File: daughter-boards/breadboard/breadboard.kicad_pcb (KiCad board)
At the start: 2 copper layers, 30 x 92 mm, 54 parts, among them P1 SAMTEC-QSE-020-01-F-D-A, P2 SAMTEC-QSE-020-01-F-D-A

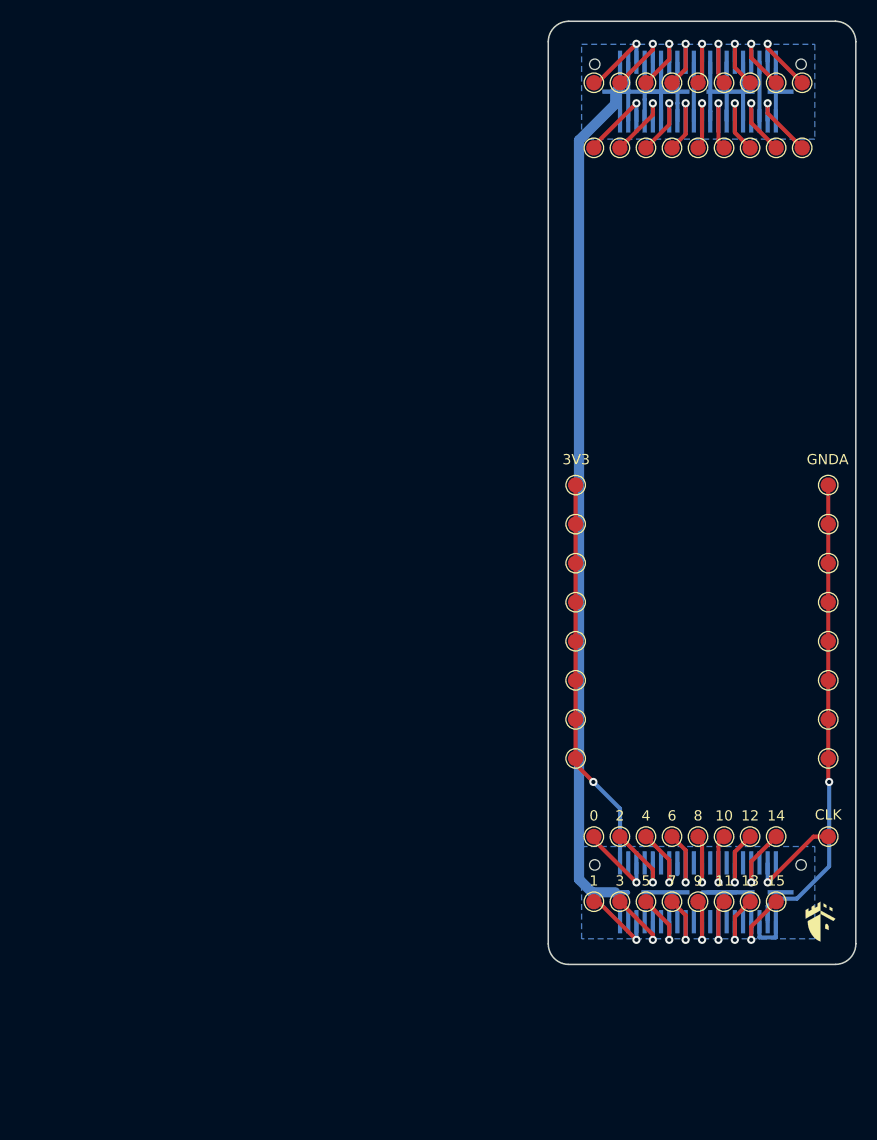
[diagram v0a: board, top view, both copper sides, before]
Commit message: Updated daughterboards for the new Scaffold socket
Update breadboard, smartcard and STM32F205 daughterboards to fit the
new socket format of Scaffold v1.1 hardware.
Previous socket format is now deprecated.
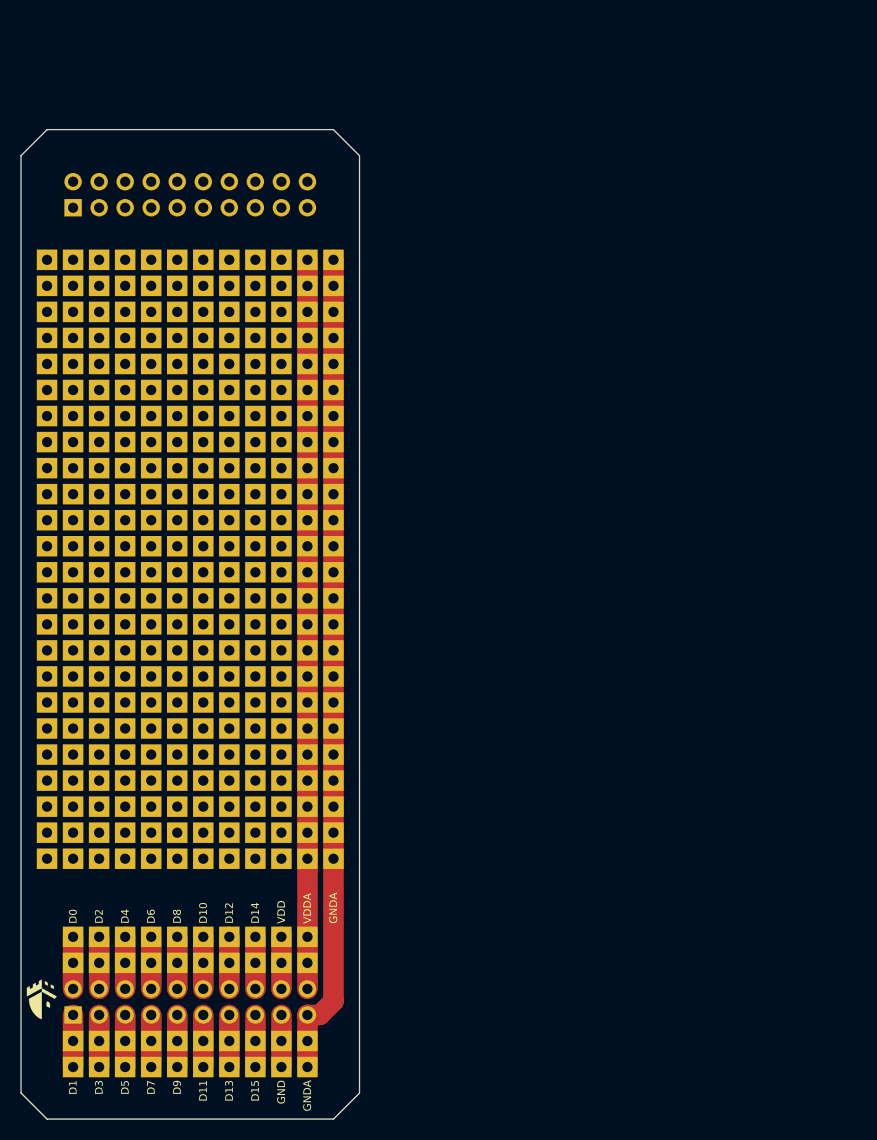
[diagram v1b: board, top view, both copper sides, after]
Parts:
- removed G***: LOGO, mykicadlibs:donjon-3000
- removed P1, P2: SAMTEC-QSE-020-01-F-D-A, mykicadlibs:SAMTEC-QSE-020-01-F-D-A
- added J1: Conn_02x10_Odd_Even, Connector_PinSocket_2.54mm:PinSocket_2x10_P2.54mm_Vertical, B.Cu at (50.8, 154.9)
- added J2: Conn_02x10_Odd_Even, Connector_PinSocket_2.54mm:PinSocket_2x10_P2.54mm_Vertical, B.Cu at (50.8, 76.2)
- added LOGO1: DUNGEON_LOGO, mykicadlibs:donjon-3000, F.Cu at (47.8, 153.4)
- added TP100: TestPoint, mykicadlibs:TEST_BREADBOARD_RECTANGULAR, F.Cu at (48.3, 81.3)
- added TP101: TestPoint, mykicadlibs:TEST_BREADBOARD_RECTANGULAR, F.Cu at (50.8, 96.5)
- added TP102: TestPoint, mykicadlibs:TEST_BREADBOARD_RECTANGULAR, F.Cu at (50.8, 86.4)
- added TP103: TestPoint, mykicadlibs:TEST_BREADBOARD_RECTANGULAR, F.Cu at (50.8, 116.8)
- added TP104: TestPoint, mykicadlibs:TEST_BREADBOARD_RECTANGULAR, F.Cu at (50.8, 101.6)
- added TP105: TestPoint, mykicadlibs:TEST_BREADBOARD_RECTANGULAR, F.Cu at (50.8, 88.9)
- added TP106: TestPoint, mykicadlibs:TEST_BREADBOARD_RECTANGULAR, F.Cu at (50.8, 91.4)
- added TP107: TestPoint, mykicadlibs:TEST_BREADBOARD_RECTANGULAR, F.Cu at (50.8, 111.8)
- added TP108: TestPoint, mykicadlibs:TEST_BREADBOARD_RECTANGULAR, F.Cu at (50.8, 121.9)
- added TP109: TestPoint, mykicadlibs:TEST_BREADBOARD_RECTANGULAR, F.Cu at (50.8, 129.5)
- added TP110: TestPoint, mykicadlibs:TEST_BREADBOARD_RECTANGULAR, F.Cu at (50.8, 81.3)
- added TP111: TestPoint, mykicadlibs:TEST_BREADBOARD_RECTANGULAR, F.Cu at (50.8, 99.1)
- added TP112: TestPoint, mykicadlibs:TEST_BREADBOARD_RECTANGULAR, F.Cu at (50.8, 119.4)
- added TP113: TestPoint, mykicadlibs:TEST_BREADBOARD_RECTANGULAR, F.Cu at (50.8, 124.5)
- added TP114: TestPoint, mykicadlibs:TEST_BREADBOARD_RECTANGULAR, F.Cu at (50.8, 94.0)
- added TP115: TestPoint, mykicadlibs:TEST_BREADBOARD_RECTANGULAR, F.Cu at (50.8, 104.1)
- added TP116: TestPoint, mykicadlibs:TEST_BREADBOARD_RECTANGULAR, F.Cu at (50.8, 114.3)
- added TP117: TestPoint, mykicadlibs:TEST_BREADBOARD_RECTANGULAR, F.Cu at (50.8, 127.0)
- added TP118: TestPoint, mykicadlibs:TEST_BREADBOARD_RECTANGULAR, F.Cu at (50.8, 83.8)
- added TP119: TestPoint, mykicadlibs:TEST_BREADBOARD_RECTANGULAR, F.Cu at (50.8, 106.7)
- added TP120: TestPoint, mykicadlibs:TEST_BREADBOARD_RECTANGULAR, F.Cu at (50.8, 109.2)
- added TP121: TestPoint, mykicadlibs:TEST_BREADBOARD_RECTANGULAR, F.Cu at (53.3, 91.4)
- added TP122: TestPoint, mykicadlibs:TEST_BREADBOARD_RECTANGULAR, F.Cu at (53.3, 114.3)
- added TP123: TestPoint, mykicadlibs:TEST_BREADBOARD_RECTANGULAR, F.Cu at (53.3, 88.9)
- added TP124: TestPoint, mykicadlibs:TEST_BREADBOARD_RECTANGULAR, F.Cu at (53.3, 94.0)
- added TP125: TestPoint, mykicadlibs:TEST_BREADBOARD_RECTANGULAR, F.Cu at (53.3, 121.9)
- added TP126: TestPoint, mykicadlibs:TEST_BREADBOARD_RECTANGULAR, F.Cu at (53.3, 116.8)
- added TP127: TestPoint, mykicadlibs:TEST_BREADBOARD_RECTANGULAR, F.Cu at (53.3, 104.1)
- added TP128: TestPoint, mykicadlibs:TEST_BREADBOARD_RECTANGULAR, F.Cu at (53.3, 86.4)
- added TP129: TestPoint, mykicadlibs:TEST_BREADBOARD_RECTANGULAR, F.Cu at (53.3, 127.0)
- added TP130: TestPoint, mykicadlibs:TEST_BREADBOARD_RECTANGULAR, F.Cu at (53.3, 111.8)
- added TP131: TestPoint, mykicadlibs:TEST_BREADBOARD_RECTANGULAR, F.Cu at (53.3, 96.5)
- added TP132: TestPoint, mykicadlibs:TEST_BREADBOARD_RECTANGULAR, F.Cu at (53.3, 83.8)
- added TP133: TestPoint, mykicadlibs:TEST_BREADBOARD_RECTANGULAR, F.Cu at (53.3, 124.5)
- added TP134: TestPoint, mykicadlibs:TEST_BREADBOARD_RECTANGULAR, F.Cu at (53.3, 119.4)
- added TP135: TestPoint, mykicadlibs:TEST_BREADBOARD_RECTANGULAR, F.Cu at (53.3, 101.6)
- added TP136: TestPoint, mykicadlibs:TEST_BREADBOARD_RECTANGULAR, F.Cu at (53.3, 81.3)
- added TP137: TestPoint, mykicadlibs:TEST_BREADBOARD_RECTANGULAR, F.Cu at (53.3, 129.5)
- added TP138: TestPoint, mykicadlibs:TEST_BREADBOARD_RECTANGULAR, F.Cu at (53.3, 106.7)
- added TP139: TestPoint, mykicadlibs:TEST_BREADBOARD_RECTANGULAR, F.Cu at (53.3, 109.2)
- added TP140: TestPoint, mykicadlibs:TEST_BREADBOARD_RECTANGULAR, F.Cu at (53.3, 99.1)
- added TP141: TestPoint, mykicadlibs:TEST_BREADBOARD_RECTANGULAR, F.Cu at (55.9, 116.8)
- added TP142: TestPoint, mykicadlibs:TEST_BREADBOARD_RECTANGULAR, F.Cu at (55.9, 94.0)
- added TP143: TestPoint, mykicadlibs:TEST_BREADBOARD_RECTANGULAR, F.Cu at (55.9, 109.2)
- added TP144: TestPoint, mykicadlibs:TEST_BREADBOARD_RECTANGULAR, F.Cu at (55.9, 104.1)
- added TP145: TestPoint, mykicadlibs:TEST_BREADBOARD_RECTANGULAR, F.Cu at (55.9, 83.8)
- added TP146: TestPoint, mykicadlibs:TEST_BREADBOARD_RECTANGULAR, F.Cu at (55.9, 127.0)
- added TP147: TestPoint, mykicadlibs:TEST_BREADBOARD_RECTANGULAR, F.Cu at (55.9, 114.3)
- added TP148: TestPoint, mykicadlibs:TEST_BREADBOARD_RECTANGULAR, F.Cu at (55.9, 106.7)
- added TP149: TestPoint, mykicadlibs:TEST_BREADBOARD_RECTANGULAR, F.Cu at (55.9, 86.4)
- added TP150: TestPoint, mykicadlibs:TEST_BREADBOARD_RECTANGULAR, F.Cu at (55.9, 124.5)
- added TP151: TestPoint, mykicadlibs:TEST_BREADBOARD_RECTANGULAR, F.Cu at (55.9, 91.4)
- added TP152: TestPoint, mykicadlibs:TEST_BREADBOARD_RECTANGULAR, F.Cu at (55.9, 101.6)
- added TP153: TestPoint, mykicadlibs:TEST_BREADBOARD_RECTANGULAR, F.Cu at (55.9, 88.9)
- added TP154: TestPoint, mykicadlibs:TEST_BREADBOARD_RECTANGULAR, F.Cu at (55.9, 129.5)
- added TP155: TestPoint, mykicadlibs:TEST_BREADBOARD_RECTANGULAR, F.Cu at (55.9, 111.8)
- added TP156: TestPoint, mykicadlibs:TEST_BREADBOARD_RECTANGULAR, F.Cu at (55.9, 99.1)
- added TP157: TestPoint, mykicadlibs:TEST_BREADBOARD_RECTANGULAR, F.Cu at (55.9, 96.5)
- added TP158: TestPoint, mykicadlibs:TEST_BREADBOARD_RECTANGULAR, F.Cu at (55.9, 121.9)
- added TP159: TestPoint, mykicadlibs:TEST_BREADBOARD_RECTANGULAR, F.Cu at (55.9, 81.3)
- added TP160: TestPoint, mykicadlibs:TEST_BREADBOARD_RECTANGULAR, F.Cu at (55.9, 119.4)
- added TP161: TestPoint, mykicadlibs:TEST_BREADBOARD_RECTANGULAR, F.Cu at (58.4, 114.3)
- added TP162: TestPoint, mykicadlibs:TEST_BREADBOARD_RECTANGULAR, F.Cu at (58.4, 101.6)
- added TP163: TestPoint, mykicadlibs:TEST_BREADBOARD_RECTANGULAR, F.Cu at (58.4, 91.4)
- added TP164: TestPoint, mykicadlibs:TEST_BREADBOARD_RECTANGULAR, F.Cu at (58.4, 127.0)
- added TP165: TestPoint, mykicadlibs:TEST_BREADBOARD_RECTANGULAR, F.Cu at (58.4, 116.8)
- added TP166: TestPoint, mykicadlibs:TEST_BREADBOARD_RECTANGULAR, F.Cu at (58.4, 96.5)
- added TP167: TestPoint, mykicadlibs:TEST_BREADBOARD_RECTANGULAR, F.Cu at (58.4, 83.8)
- added TP168: TestPoint, mykicadlibs:TEST_BREADBOARD_RECTANGULAR, F.Cu at (58.4, 124.5)
- added TP169: TestPoint, mykicadlibs:TEST_BREADBOARD_RECTANGULAR, F.Cu at (58.4, 111.8)
- added TP170: TestPoint, mykicadlibs:TEST_BREADBOARD_RECTANGULAR, F.Cu at (58.4, 104.1)
- added TP171: TestPoint, mykicadlibs:TEST_BREADBOARD_RECTANGULAR, F.Cu at (58.4, 99.1)
- added TP172: TestPoint, mykicadlibs:TEST_BREADBOARD_RECTANGULAR, F.Cu at (58.4, 81.3)
- added TP173: TestPoint, mykicadlibs:TEST_BREADBOARD_RECTANGULAR, F.Cu at (58.4, 121.9)
- added TP174: TestPoint, mykicadlibs:TEST_BREADBOARD_RECTANGULAR, F.Cu at (58.4, 109.2)
- added TP175: TestPoint, mykicadlibs:TEST_BREADBOARD_RECTANGULAR, F.Cu at (58.4, 106.7)
- added TP176: TestPoint, mykicadlibs:TEST_BREADBOARD_RECTANGULAR, F.Cu at (58.4, 88.9)
- added TP177: TestPoint, mykicadlibs:TEST_BREADBOARD_RECTANGULAR, F.Cu at (58.4, 129.5)
- added TP178: TestPoint, mykicadlibs:TEST_BREADBOARD_RECTANGULAR, F.Cu at (58.4, 94.0)
- added TP179: TestPoint, mykicadlibs:TEST_BREADBOARD_RECTANGULAR, F.Cu at (58.4, 119.4)
- added TP180: TestPoint, mykicadlibs:TEST_BREADBOARD_RECTANGULAR, F.Cu at (58.4, 86.4)
- added TP181: TestPoint, mykicadlibs:TEST_BREADBOARD_RECTANGULAR, F.Cu at (61.0, 96.5)
- added TP182: TestPoint, mykicadlibs:TEST_BREADBOARD_RECTANGULAR, F.Cu at (61.0, 111.8)
- added TP183: TestPoint, mykicadlibs:TEST_BREADBOARD_RECTANGULAR, F.Cu at (61.0, 101.6)
- added TP184: TestPoint, mykicadlibs:TEST_BREADBOARD_RECTANGULAR, F.Cu at (61.0, 91.4)
- added TP185: TestPoint, mykicadlibs:TEST_BREADBOARD_RECTANGULAR, F.Cu at (61.0, 121.9)
- added TP186: TestPoint, mykicadlibs:TEST_BREADBOARD_RECTANGULAR, F.Cu at (61.0, 114.3)
- added TP187: TestPoint, mykicadlibs:TEST_BREADBOARD_RECTANGULAR, F.Cu at (61.0, 81.3)
- added TP188: TestPoint, mykicadlibs:TEST_BREADBOARD_RECTANGULAR, F.Cu at (61.0, 94.0)
- added TP189: TestPoint, mykicadlibs:TEST_BREADBOARD_RECTANGULAR, F.Cu at (61.0, 86.4)
- added TP190: TestPoint, mykicadlibs:TEST_BREADBOARD_RECTANGULAR, F.Cu at (61.0, 127.0)
- added TP191: TestPoint, mykicadlibs:TEST_BREADBOARD_RECTANGULAR, F.Cu at (61.0, 119.4)
- added TP192: TestPoint, mykicadlibs:TEST_BREADBOARD_RECTANGULAR, F.Cu at (61.0, 99.1)
- added TP193: TestPoint, mykicadlibs:TEST_BREADBOARD_RECTANGULAR, F.Cu at (61.0, 83.8)
- added TP194: TestPoint, mykicadlibs:TEST_BREADBOARD_RECTANGULAR, F.Cu at (61.0, 124.5)
- added TP195: TestPoint, mykicadlibs:TEST_BREADBOARD_RECTANGULAR, F.Cu at (61.0, 109.2)
- added TP196: TestPoint, mykicadlibs:TEST_BREADBOARD_RECTANGULAR, F.Cu at (61.0, 106.7)
- added TP197: TestPoint, mykicadlibs:TEST_BREADBOARD_RECTANGULAR, F.Cu at (61.0, 88.9)
- added TP198: TestPoint, mykicadlibs:TEST_BREADBOARD_RECTANGULAR, F.Cu at (61.0, 129.5)
- added TP199: TestPoint, mykicadlibs:TEST_BREADBOARD_RECTANGULAR, F.Cu at (61.0, 104.1)
- added TP200: TestPoint, mykicadlibs:TEST_BREADBOARD_RECTANGULAR, F.Cu at (61.0, 116.8)
- added TP201: TestPoint, mykicadlibs:TEST_BREADBOARD_RECTANGULAR, F.Cu at (63.5, 114.3)
- added TP202: TestPoint, mykicadlibs:TEST_BREADBOARD_RECTANGULAR, F.Cu at (63.5, 99.1)
- added TP203: TestPoint, mykicadlibs:TEST_BREADBOARD_RECTANGULAR, F.Cu at (63.5, 88.9)
- added TP204: TestPoint, mykicadlibs:TEST_BREADBOARD_RECTANGULAR, F.Cu at (63.5, 96.5)
- added TP205: TestPoint, mykicadlibs:TEST_BREADBOARD_RECTANGULAR, F.Cu at (63.5, 119.4)
- added TP206: TestPoint, mykicadlibs:TEST_BREADBOARD_RECTANGULAR, F.Cu at (63.5, 109.2)
- added TP207: TestPoint, mykicadlibs:TEST_BREADBOARD_RECTANGULAR, F.Cu at (63.5, 106.7)
- added TP208: TestPoint, mykicadlibs:TEST_BREADBOARD_RECTANGULAR, F.Cu at (63.5, 81.3)
- added TP209: TestPoint, mykicadlibs:TEST_BREADBOARD_RECTANGULAR, F.Cu at (63.5, 124.5)
- added TP210: TestPoint, mykicadlibs:TEST_BREADBOARD_RECTANGULAR, F.Cu at (63.5, 111.8)
- added TP211: TestPoint, mykicadlibs:TEST_BREADBOARD_RECTANGULAR, F.Cu at (63.5, 104.1)
- added TP212: TestPoint, mykicadlibs:TEST_BREADBOARD_RECTANGULAR, F.Cu at (63.5, 86.4)
- added TP213: TestPoint, mykicadlibs:TEST_BREADBOARD_RECTANGULAR, F.Cu at (63.5, 121.9)
- added TP214: TestPoint, mykicadlibs:TEST_BREADBOARD_RECTANGULAR, F.Cu at (63.5, 129.5)
- added TP215: TestPoint, mykicadlibs:TEST_BREADBOARD_RECTANGULAR, F.Cu at (63.5, 101.6)
- added TP216: TestPoint, mykicadlibs:TEST_BREADBOARD_RECTANGULAR, F.Cu at (63.5, 91.4)
- added TP217: TestPoint, mykicadlibs:TEST_BREADBOARD_RECTANGULAR, F.Cu at (63.5, 127.0)
- added TP218: TestPoint, mykicadlibs:TEST_BREADBOARD_RECTANGULAR, F.Cu at (63.5, 94.0)
- added TP219: TestPoint, mykicadlibs:TEST_BREADBOARD_RECTANGULAR, F.Cu at (63.5, 116.8)
- added TP220: TestPoint, mykicadlibs:TEST_BREADBOARD_RECTANGULAR, F.Cu at (63.5, 83.8)
- added TP221: TestPoint, mykicadlibs:TEST_BREADBOARD_RECTANGULAR, F.Cu at (66.0, 81.3)
- added TP222: TestPoint, mykicadlibs:TEST_BREADBOARD_RECTANGULAR, F.Cu at (66.0, 119.4)
- added TP223: TestPoint, mykicadlibs:TEST_BREADBOARD_RECTANGULAR, F.Cu at (66.0, 96.5)
- added TP224: TestPoint, mykicadlibs:TEST_BREADBOARD_RECTANGULAR, F.Cu at (66.0, 83.8)
- added TP225: TestPoint, mykicadlibs:TEST_BREADBOARD_RECTANGULAR, F.Cu at (66.0, 111.8)
- added TP226: TestPoint, mykicadlibs:TEST_BREADBOARD_RECTANGULAR, F.Cu at (66.0, 91.4)
- added TP227: TestPoint, mykicadlibs:TEST_BREADBOARD_RECTANGULAR, F.Cu at (66.0, 129.5)
- added TP228: TestPoint, mykicadlibs:TEST_BREADBOARD_RECTANGULAR, F.Cu at (66.0, 94.0)
- added TP229: TestPoint, mykicadlibs:TEST_BREADBOARD_RECTANGULAR, F.Cu at (66.0, 104.1)
- added TP230: TestPoint, mykicadlibs:TEST_BREADBOARD_RECTANGULAR, F.Cu at (66.0, 114.3)
- added TP231: TestPoint, mykicadlibs:TEST_BREADBOARD_RECTANGULAR, F.Cu at (66.0, 121.9)
- added TP232: TestPoint, mykicadlibs:TEST_BREADBOARD_RECTANGULAR, F.Cu at (66.0, 88.9)
- added TP233: TestPoint, mykicadlibs:TEST_BREADBOARD_RECTANGULAR, F.Cu at (66.0, 99.1)
- added TP234: TestPoint, mykicadlibs:TEST_BREADBOARD_RECTANGULAR, F.Cu at (66.0, 109.2)
- added TP235: TestPoint, mykicadlibs:TEST_BREADBOARD_RECTANGULAR, F.Cu at (66.0, 124.5)
- added TP236: TestPoint, mykicadlibs:TEST_BREADBOARD_RECTANGULAR, F.Cu at (66.0, 86.4)
- added TP237: TestPoint, mykicadlibs:TEST_BREADBOARD_RECTANGULAR, F.Cu at (66.0, 101.6)
- added TP238: TestPoint, mykicadlibs:TEST_BREADBOARD_RECTANGULAR, F.Cu at (66.0, 116.8)
- added TP239: TestPoint, mykicadlibs:TEST_BREADBOARD_RECTANGULAR, F.Cu at (66.0, 106.7)
- added TP240: TestPoint, mykicadlibs:TEST_BREADBOARD_RECTANGULAR, F.Cu at (66.0, 127.0)
- added TP241: TestPoint, mykicadlibs:TEST_BREADBOARD_RECTANGULAR, F.Cu at (68.6, 83.8)
- added TP242: TestPoint, mykicadlibs:TEST_BREADBOARD_RECTANGULAR, F.Cu at (68.6, 99.1)
- added TP243: TestPoint, mykicadlibs:TEST_BREADBOARD_RECTANGULAR, F.Cu at (68.6, 116.8)
- added TP244: TestPoint, mykicadlibs:TEST_BREADBOARD_RECTANGULAR, F.Cu at (68.6, 94.0)
- added TP245: TestPoint, mykicadlibs:TEST_BREADBOARD_RECTANGULAR, F.Cu at (68.6, 127.0)
- added TP246: TestPoint, mykicadlibs:TEST_BREADBOARD_RECTANGULAR, F.Cu at (68.6, 114.3)
- added TP247: TestPoint, mykicadlibs:TEST_BREADBOARD_RECTANGULAR, F.Cu at (68.6, 129.5)
- added TP248: TestPoint, mykicadlibs:TEST_BREADBOARD_RECTANGULAR, F.Cu at (68.6, 88.9)
- added TP249: TestPoint, mykicadlibs:TEST_BREADBOARD_RECTANGULAR, F.Cu at (68.6, 104.1)
- added TP250: TestPoint, mykicadlibs:TEST_BREADBOARD_RECTANGULAR, F.Cu at (68.6, 111.8)
- added TP251: TestPoint, mykicadlibs:TEST_BREADBOARD_RECTANGULAR, F.Cu at (68.6, 124.5)
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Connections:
- TP1 pad 1: Net-(P1-Pad4) -> VDDA
- TP10 pad 1: Net-(P1-Pad8) -> VDDA
- TP11 pad 1: Net-(P1-Pad12) -> VDDA
- TP12 pad 1: Net-(P1-Pad16) -> VDDA
- TP13 pad 1: Net-(P1-Pad20) -> VDDA
- TP14 pad 1: Net-(P1-Pad24) -> VDDA
- TP15 pad 1: Net-(P1-Pad28) -> VDDA
- TP16 pad 1: Net-(P1-Pad32) -> VDDA
- TP17 pad 1: Net-(P1-Pad36) -> VDDA
- TP18 pad 1: GNDA -> VDDA
- TP19 pad 1: GNDA -> VDDA
- TP2 pad 1: Net-(P1-Pad7) -> VDDA
- TP20 pad 1: GNDA -> VDDA
- TP21 pad 1: GNDA -> /D2
- TP22 pad 1: GNDA -> /D2
- TP23 pad 1: GNDA -> /D3
- TP24 pad 1: GNDA -> /D3
- TP25 pad 1: GNDA -> /D4
- TP26 pad 1: +3V3 -> /D4
- TP27 pad 1: +3V3 -> GNDA
- TP28 pad 1: +3V3 -> GNDA
- TP29 pad 1: +3V3 -> GNDA
- TP3 pad 1: Net-(P1-Pad11) -> VDDA
- TP30 pad 1: +3V3 -> GNDA
- TP31 pad 1: +3V3 -> GNDA
- TP32 pad 1: +3V3 -> GNDA
- TP33 pad 1: +3V3 -> GNDA
- TP34 pad 1: Net-(P2-Pad3) -> GNDA
- TP35 pad 1: Net-(P2-Pad7) -> GNDA
- TP36 pad 1: Net-(P2-Pad11) -> GNDA
- TP37 pad 1: Net-(P2-Pad15) -> GNDA
- TP38 pad 1: Net-(P2-Pad19) -> GNDA
- TP39 pad 1: Net-(P2-Pad23) -> GNDA
- TP4 pad 1: Net-(P1-Pad15) -> VDDA
- TP40 pad 1: Net-(P2-Pad27) -> GNDA
- TP41 pad 1: Net-(P2-Pad31) -> GNDA
- TP42 pad 1: Net-(P2-Pad35) -> GNDA
- TP43 pad 1: Net-(P2-Pad4) -> GNDA
- TP44 pad 1: Net-(P2-Pad8) -> GNDA
- TP45 pad 1: Net-(P2-Pad12) -> GNDA
- TP46 pad 1: Net-(P2-Pad16) -> GNDA
- TP47 pad 1: Net-(P2-Pad20) -> /D5
- TP48 pad 1: Net-(P2-Pad24) -> /D5
- TP49 pad 1: Net-(P2-Pad28) -> /D6
- TP5 pad 1: Net-(P1-Pad19) -> VDDA
- TP50 pad 1: Net-(P2-Pad32) -> /D6
- TP51 pad 1: Net-(P2-Pad36) -> /D7
- TP6 pad 1: Net-(P1-Pad23) -> VDDA
- TP7 pad 1: Net-(P1-Pad27) -> VDDA
- TP8 pad 1: Net-(P1-Pad31) -> VDDA
- TP9 pad 1: Net-(P1-Pad35) -> VDDA
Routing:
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- removed copper zone on B.Cu, net GND
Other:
- board size 30 x 92 mm -> 33 x 96.5 mm
- rule pad_to_mask_clearance: 0.2 -> 0
- board text added: "D0"
- board text added: "D1"
- board text added: "D10"
- board text added: "D11"
- board text added: "D12"
- board text added: "D13"
- board text added: "D14"
- board text added: "D15"
- board text added: "D2"
- board text added: "D3"
- board text added: "D4"
- board text added: "D5"
- board text added: "D6"
- board text added: "D7"
- board text added: "D8"
- board text added: "D9"
- board text added: "GND"
- board text added: "VDD"
- board text added: "VDDA"
- board text removed: "0"
- board text removed: "1"
- board text removed: "10"
- board text removed: "11"
- board text removed: "12"
- board text removed: "13"
- board text removed: "14"
- board text removed: "15"
- board text removed: "2"
- board text removed: "3"
- board text removed: "3V3"
- board text removed: "4"
- board text removed: "5"
- board text removed: "6"
- board text removed: "7"
- board text removed: "8"
- board text removed: "9"
- board text removed: "CLK"

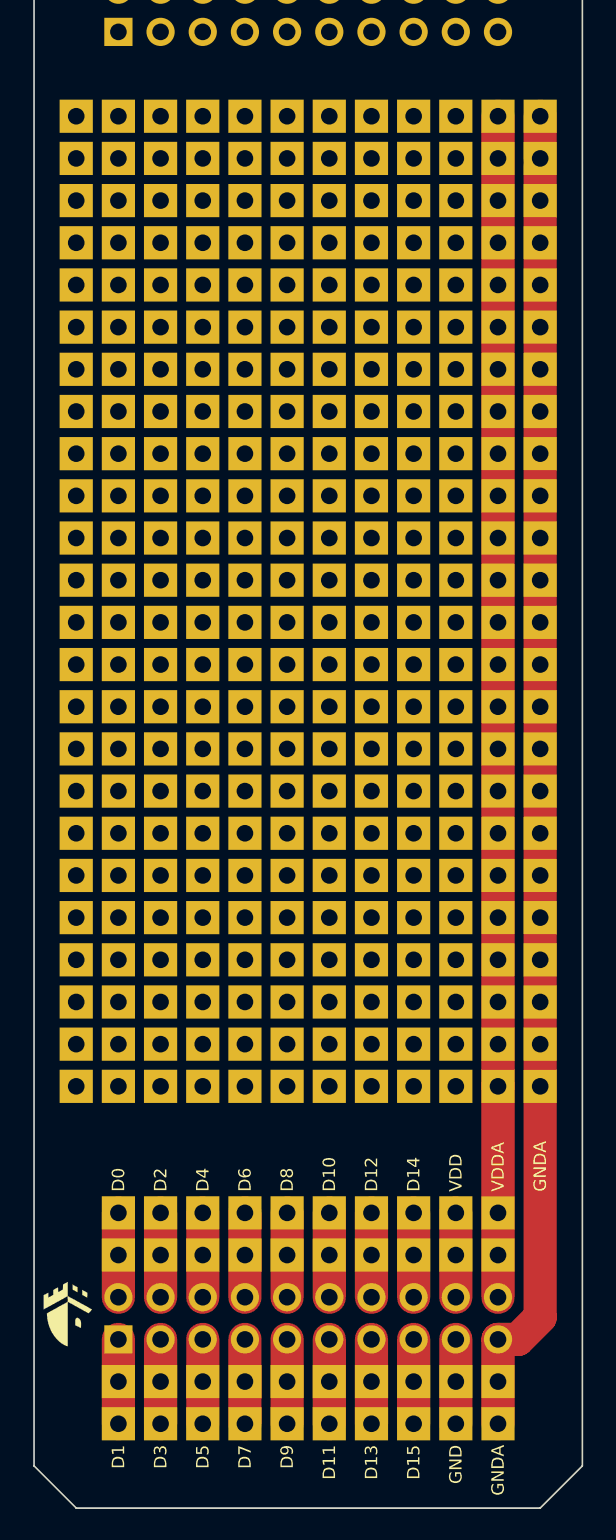
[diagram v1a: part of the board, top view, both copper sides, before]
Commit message: Fixed holes in breadboard daughterboard.
Replaced plated holes with non-plated holes for easier solderability.
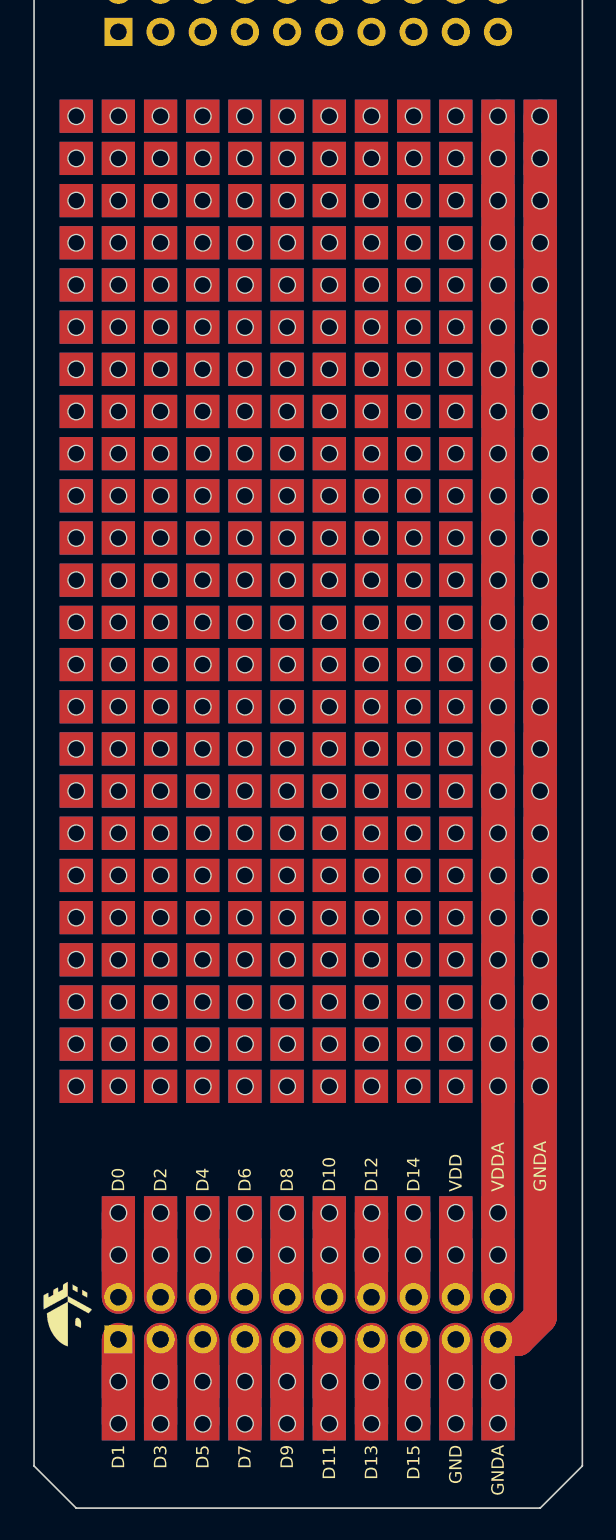
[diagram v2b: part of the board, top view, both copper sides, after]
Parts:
- removed TP1, TP10, TP100, TP101, TP102, TP103, TP104, TP105, TP106, TP107, TP108, TP109, TP11, TP110, TP111, TP112, TP113, TP114, TP115, TP116, TP117, TP118, TP119, TP12, TP120, TP121, TP122, TP123, TP124, TP125, TP126, TP127, TP128, TP129, TP13, TP130, TP131, TP132, TP133, TP134, TP135, TP136, TP137, TP138, TP139, TP14, TP140, TP141, TP142, TP143, TP144, TP145, TP146, TP147, TP148, TP149, TP15, TP150, TP151, TP152, TP153, TP154, TP155, TP156, TP157, TP158, TP159, TP16, TP160, TP161, TP162, TP163, TP164, TP165, TP166, TP167, TP168, TP169, TP17, TP170, TP171, TP172, TP173, TP174, TP175, TP176, TP177, TP178, TP179, TP18, TP180, TP181, TP182, TP183, TP184, TP185, TP186, TP187, TP188, TP189, TP19, TP190, TP191, TP192, TP193, TP194, TP195, TP196, TP197, TP198, TP199, TP2, TP20, TP200, TP201, TP202, TP203, TP204, TP205, TP206, TP207, TP208, TP209, TP21, TP210, TP211, TP212, TP213, TP214, TP215, TP216, TP217, TP218, TP219, TP22, TP220, TP221, TP222, TP223, TP224, TP225, TP226, TP227, TP228, TP229, TP23, TP230, TP231, TP232, TP233, TP234, TP235, TP236, TP237, TP238, TP239, TP24, TP240, TP241, TP242, TP243, TP244, TP245, TP246, TP247, TP248, TP249, TP25, TP250, TP251, TP252, TP253, TP254, TP255, TP256, TP257, TP258, TP259, TP26, TP260, TP261, TP262, TP263, TP264, TP265, TP266, TP267, TP268, TP269, TP27, TP270, TP271, TP272, TP273, TP274, TP275, TP276, TP277, TP278, TP279, TP28, TP280, TP281, TP282, TP283, TP284, TP285, TP286, TP287, TP288, TP289, TP29, TP290, TP291, TP292, TP293, TP294, TP295, TP296, TP297, TP298, TP299, TP3, TP30, TP300, TP301, TP302, TP303, TP304, TP305, TP306, TP307, TP308, TP309, TP31, TP310, TP311, TP312, TP313, TP314, TP315, TP316, TP317, TP318, TP319, TP32, TP320, TP321, TP322, TP323, TP324, TP325, TP326, TP327, TP328, TP33, TP34, TP35, TP36, TP37, TP38, TP39, TP4, TP40, TP41, TP42, TP43, TP44, TP45, TP46, TP47, TP48, TP49, TP5, TP50, TP51, TP52, TP53, TP54, TP55, TP56, TP57, TP58, TP59, TP6, TP60, TP61, TP62, TP63, TP64, TP65, TP66, TP67, TP68, TP69, TP7, TP70, TP71, TP72, TP73, TP74, TP75, TP76, TP77, TP78, TP79, TP8, TP80, TP81, TP82, TP83, TP84, TP85, TP86, TP87, TP88, TP89, TP9, TP90, TP91, TP92, TP93, TP94, TP95, TP96, TP97, TP98, TP99: TestPoint, mykicadlibs:TEST_BREADBOARD_RECTANGULAR
- added U1: BREADBOARD_NPTH, mykicadlibs:TEST_BREADBOARD_RECTANGULAR_NPTH2, F.Cu at (48.3, 83.8)
- added U10: BREADBOARD_NPTH, mykicadlibs:TEST_BREADBOARD_RECTANGULAR_NPTH2, F.Cu at (48.3, 96.5)
- added U100: BREADBOARD_NPTH, mykicadlibs:TEST_BREADBOARD_RECTANGULAR_NPTH2, F.Cu at (66.0, 81.3)
- added U101: BREADBOARD_NPTH, mykicadlibs:TEST_BREADBOARD_RECTANGULAR_NPTH2, F.Cu at (71.1, 139.7)
- added U102: BREADBOARD_NPTH, mykicadlibs:TEST_BREADBOARD_RECTANGULAR_NPTH2, F.Cu at (48.3, 116.8)
- added U103: BREADBOARD_NPTH, mykicadlibs:TEST_BREADBOARD_RECTANGULAR_NPTH2, F.Cu at (50.8, 134.6)
- added U104: BREADBOARD_NPTH, mykicadlibs:TEST_BREADBOARD_RECTANGULAR_NPTH2, F.Cu at (50.8, 86.4)
- added U105: BREADBOARD_NPTH, mykicadlibs:TEST_BREADBOARD_RECTANGULAR_NPTH2, F.Cu at (53.3, 83.8)
- added U106: BREADBOARD_NPTH, mykicadlibs:TEST_BREADBOARD_RECTANGULAR_NPTH2, F.Cu at (48.3, 109.2)
- added U107: BREADBOARD_NPTH, mykicadlibs:TEST_BREADBOARD_RECTANGULAR_NPTH2, F.Cu at (53.3, 101.6)
- added U108: BREADBOARD_NPTH, mykicadlibs:TEST_BREADBOARD_RECTANGULAR_NPTH2, F.Cu at (63.5, 86.4)
- added U109: BREADBOARD_NPTH, mykicadlibs:TEST_BREADBOARD_RECTANGULAR_NPTH2, F.Cu at (61.0, 111.8)
- added U11: BREADBOARD_NPTH, mykicadlibs:TEST_BREADBOARD_RECTANGULAR_NPTH2, F.Cu at (71.1, 104.1)
- added U110: BREADBOARD_NPTH, mykicadlibs:TEST_BREADBOARD_RECTANGULAR_NPTH2, F.Cu at (63.5, 94.0)
- added U111: BREADBOARD_NPTH, mykicadlibs:TEST_BREADBOARD_RECTANGULAR_NPTH2, F.Cu at (66.0, 104.1)
- added U112: BREADBOARD_NPTH, mykicadlibs:TEST_BREADBOARD_RECTANGULAR_NPTH2, F.Cu at (68.6, 124.5)
- added U113: BREADBOARD_NPTH, mykicadlibs:TEST_BREADBOARD_RECTANGULAR_NPTH2, F.Cu at (68.6, 88.9)
- added U114: BREADBOARD_NPTH, mykicadlibs:TEST_BREADBOARD_RECTANGULAR_NPTH2, F.Cu at (71.1, 83.8)
- added U115: BREADBOARD_NPTH, mykicadlibs:TEST_BREADBOARD_RECTANGULAR_NPTH2, F.Cu at (50.8, 132.1)
- added U116: BREADBOARD_NPTH, mykicadlibs:TEST_BREADBOARD_RECTANGULAR_NPTH2, F.Cu at (50.8, 94.0)
- added U117: BREADBOARD_NPTH, mykicadlibs:TEST_BREADBOARD_RECTANGULAR_NPTH2, F.Cu at (58.4, 94.0)
- added U118: BREADBOARD_NPTH, mykicadlibs:TEST_BREADBOARD_RECTANGULAR_NPTH2, F.Cu at (58.4, 114.3)
- added U119: BREADBOARD_NPTH, mykicadlibs:TEST_BREADBOARD_RECTANGULAR_NPTH2, F.Cu at (61.0, 129.5)
- added U12: BREADBOARD_NPTH, mykicadlibs:TEST_BREADBOARD_RECTANGULAR_NPTH2, F.Cu at (68.6, 111.8)
- added U120: BREADBOARD_NPTH, mykicadlibs:TEST_BREADBOARD_RECTANGULAR_NPTH2, F.Cu at (61.0, 88.9)
- added U121: BREADBOARD_NPTH, mykicadlibs:TEST_BREADBOARD_RECTANGULAR_NPTH2, F.Cu at (63.5, 104.1)
- added U122: BREADBOARD_NPTH, mykicadlibs:TEST_BREADBOARD_RECTANGULAR_NPTH2, F.Cu at (66.0, 129.5)
- added U123: BREADBOARD_NPTH, mykicadlibs:TEST_BREADBOARD_RECTANGULAR_NPTH2, F.Cu at (68.6, 114.3)
- added U124: BREADBOARD_NPTH, mykicadlibs:TEST_BREADBOARD_RECTANGULAR_NPTH2, F.Cu at (71.1, 114.3)
- added U125: BREADBOARD_NPTH, mykicadlibs:TEST_BREADBOARD_RECTANGULAR_NPTH2, F.Cu at (71.1, 94.0)
- added U126: BREADBOARD_NPTH, mykicadlibs:TEST_BREADBOARD_RECTANGULAR_NPTH2, F.Cu at (50.8, 119.4)
- added U127: BREADBOARD_NPTH, mykicadlibs:TEST_BREADBOARD_RECTANGULAR_NPTH2, F.Cu at (61.0, 99.1)
- added U128: BREADBOARD_NPTH, mykicadlibs:TEST_BREADBOARD_RECTANGULAR_NPTH2, F.Cu at (55.9, 134.6)
- added U129: BREADBOARD_NPTH, mykicadlibs:TEST_BREADBOARD_RECTANGULAR_NPTH2, F.Cu at (55.9, 101.6)
- added U13: BREADBOARD_NPTH, mykicadlibs:TEST_BREADBOARD_RECTANGULAR_NPTH2, F.Cu at (71.1, 119.4)
- added U130: BREADBOARD_NPTH, mykicadlibs:TEST_BREADBOARD_RECTANGULAR_NPTH2, F.Cu at (55.9, 86.4)
- added U131: BREADBOARD_NPTH, mykicadlibs:TEST_BREADBOARD_RECTANGULAR_NPTH2, F.Cu at (58.4, 106.7)
- added U132: BREADBOARD_NPTH, mykicadlibs:TEST_BREADBOARD_RECTANGULAR_NPTH2, F.Cu at (61.0, 94.0)
- added U133: BREADBOARD_NPTH, mykicadlibs:TEST_BREADBOARD_RECTANGULAR_NPTH2, F.Cu at (63.5, 119.4)
- added U134: BREADBOARD_NPTH, mykicadlibs:TEST_BREADBOARD_RECTANGULAR_NPTH2, F.Cu at (66.0, 106.7)
- added U135: BREADBOARD_NPTH, mykicadlibs:TEST_BREADBOARD_RECTANGULAR_NPTH2, F.Cu at (68.6, 137.2)
- added U136: BREADBOARD_NPTH, mykicadlibs:TEST_BREADBOARD_RECTANGULAR_NPTH2, F.Cu at (71.1, 109.2)
- added U137: BREADBOARD_NPTH, mykicadlibs:TEST_BREADBOARD_RECTANGULAR_NPTH2, F.Cu at (71.1, 101.6)
- added U138: BREADBOARD_NPTH, mykicadlibs:TEST_BREADBOARD_RECTANGULAR_NPTH2, F.Cu at (68.6, 127.0)
- added U139: BREADBOARD_NPTH, mykicadlibs:TEST_BREADBOARD_RECTANGULAR_NPTH2, F.Cu at (50.8, 88.9)
- added U14: BREADBOARD_NPTH, mykicadlibs:TEST_BREADBOARD_RECTANGULAR_NPTH2, F.Cu at (48.3, 137.2)
- added U140: BREADBOARD_NPTH, mykicadlibs:TEST_BREADBOARD_RECTANGULAR_NPTH2, F.Cu at (53.3, 134.6)
- added U141: BREADBOARD_NPTH, mykicadlibs:TEST_BREADBOARD_RECTANGULAR_NPTH2, F.Cu at (53.3, 88.9)
- added U142: BREADBOARD_NPTH, mykicadlibs:TEST_BREADBOARD_RECTANGULAR_NPTH2, F.Cu at (55.9, 132.1)
- added U143: BREADBOARD_NPTH, mykicadlibs:TEST_BREADBOARD_RECTANGULAR_NPTH2, F.Cu at (55.9, 88.9)
- added U144: BREADBOARD_NPTH, mykicadlibs:TEST_BREADBOARD_RECTANGULAR_NPTH2, F.Cu at (58.4, 88.9)
- added U145: BREADBOARD_NPTH, mykicadlibs:TEST_BREADBOARD_RECTANGULAR_NPTH2, F.Cu at (61.0, 81.3)
- added U146: BREADBOARD_NPTH, mykicadlibs:TEST_BREADBOARD_RECTANGULAR_NPTH2, F.Cu at (63.5, 91.4)
- added U147: BREADBOARD_NPTH, mykicadlibs:TEST_BREADBOARD_RECTANGULAR_NPTH2, F.Cu at (66.0, 101.6)
- added U148: BREADBOARD_NPTH, mykicadlibs:TEST_BREADBOARD_RECTANGULAR_NPTH2, F.Cu at (53.3, 86.4)
- added U149: BREADBOARD_NPTH, mykicadlibs:TEST_BREADBOARD_RECTANGULAR_NPTH2, F.Cu at (50.8, 124.5)
- added U15: BREADBOARD_NPTH, mykicadlibs:TEST_BREADBOARD_RECTANGULAR_NPTH2, F.Cu at (48.3, 86.4)
- added U150: BREADBOARD_NPTH, mykicadlibs:TEST_BREADBOARD_RECTANGULAR_NPTH2, F.Cu at (48.3, 132.1)
- added U151: BREADBOARD_NPTH, mykicadlibs:TEST_BREADBOARD_RECTANGULAR_NPTH2, F.Cu at (50.8, 104.1)
- added U152: BREADBOARD_NPTH, mykicadlibs:TEST_BREADBOARD_RECTANGULAR_NPTH2, F.Cu at (50.8, 101.6)
- added U153: BREADBOARD_NPTH, mykicadlibs:TEST_BREADBOARD_RECTANGULAR_NPTH2, F.Cu at (53.3, 119.4)
- added U154: BREADBOARD_NPTH, mykicadlibs:TEST_BREADBOARD_RECTANGULAR_NPTH2, F.Cu at (55.9, 111.8)
- added U155: BREADBOARD_NPTH, mykicadlibs:TEST_BREADBOARD_RECTANGULAR_NPTH2, F.Cu at (58.4, 139.7)
- added U156: BREADBOARD_NPTH, mykicadlibs:TEST_BREADBOARD_RECTANGULAR_NPTH2, F.Cu at (58.4, 91.4)
- added U157: BREADBOARD_NPTH, mykicadlibs:TEST_BREADBOARD_RECTANGULAR_NPTH2, F.Cu at (61.0, 119.4)
- added U158: BREADBOARD_NPTH, mykicadlibs:TEST_BREADBOARD_RECTANGULAR_NPTH2, F.Cu at (63.5, 96.5)
- added U159: BREADBOARD_NPTH, mykicadlibs:TEST_BREADBOARD_RECTANGULAR_NPTH2, F.Cu at (55.9, 83.8)
- added U16: BREADBOARD_NPTH, mykicadlibs:TEST_BREADBOARD_RECTANGULAR_NPTH2, F.Cu at (66.0, 121.9)
- added U160: BREADBOARD_NPTH, mykicadlibs:TEST_BREADBOARD_RECTANGULAR_NPTH2, F.Cu at (63.5, 101.6)
- added U161: BREADBOARD_NPTH, mykicadlibs:TEST_BREADBOARD_RECTANGULAR_NPTH2, F.Cu at (66.0, 83.8)
- added U162: BREADBOARD_NPTH, mykicadlibs:TEST_BREADBOARD_RECTANGULAR_NPTH2, F.Cu at (71.1, 121.9)
- added U163: BREADBOARD_NPTH, mykicadlibs:TEST_BREADBOARD_RECTANGULAR_NPTH2, F.Cu at (71.1, 91.4)
- added U164: BREADBOARD_NPTH, mykicadlibs:TEST_BREADBOARD_RECTANGULAR_NPTH2, F.Cu at (50.8, 106.7)
- added U165: BREADBOARD_NPTH, mykicadlibs:TEST_BREADBOARD_RECTANGULAR_NPTH2, F.Cu at (53.3, 137.2)
- added U166: BREADBOARD_NPTH, mykicadlibs:TEST_BREADBOARD_RECTANGULAR_NPTH2, F.Cu at (53.3, 96.5)
- added U167: BREADBOARD_NPTH, mykicadlibs:TEST_BREADBOARD_RECTANGULAR_NPTH2, F.Cu at (61.0, 101.6)
- added U168: BREADBOARD_NPTH, mykicadlibs:TEST_BREADBOARD_RECTANGULAR_NPTH2, F.Cu at (58.4, 124.5)
- added U169: BREADBOARD_NPTH, mykicadlibs:TEST_BREADBOARD_RECTANGULAR_NPTH2, F.Cu at (58.4, 127.0)
- added U17: BREADBOARD_NPTH, mykicadlibs:TEST_BREADBOARD_RECTANGULAR_NPTH2, F.Cu at (68.6, 139.7)
- added U170: BREADBOARD_NPTH, mykicadlibs:TEST_BREADBOARD_RECTANGULAR_NPTH2, F.Cu at (63.5, 139.7)
- added U171: BREADBOARD_NPTH, mykicadlibs:TEST_BREADBOARD_RECTANGULAR_NPTH2, F.Cu at (66.0, 137.2)
- added U172: BREADBOARD_NPTH, mykicadlibs:TEST_BREADBOARD_RECTANGULAR_NPTH2, F.Cu at (66.0, 132.1)
- added U173: BREADBOARD_NPTH, mykicadlibs:TEST_BREADBOARD_RECTANGULAR_NPTH2, F.Cu at (68.6, 129.5)
- added U174: BREADBOARD_NPTH, mykicadlibs:TEST_BREADBOARD_RECTANGULAR_NPTH2, F.Cu at (68.6, 91.4)
- added U175: BREADBOARD_NPTH, mykicadlibs:TEST_BREADBOARD_RECTANGULAR_NPTH2, F.Cu at (48.3, 134.6)
- added U176: BREADBOARD_NPTH, mykicadlibs:TEST_BREADBOARD_RECTANGULAR_NPTH2, F.Cu at (50.8, 127.0)
- added U177: BREADBOARD_NPTH, mykicadlibs:TEST_BREADBOARD_RECTANGULAR_NPTH2, F.Cu at (50.8, 99.1)
- added U178: BREADBOARD_NPTH, mykicadlibs:TEST_BREADBOARD_RECTANGULAR_NPTH2, F.Cu at (53.3, 104.1)
- added U179: BREADBOARD_NPTH, mykicadlibs:TEST_BREADBOARD_RECTANGULAR_NPTH2, F.Cu at (55.9, 129.5)
- added U18: BREADBOARD_NPTH, mykicadlibs:TEST_BREADBOARD_RECTANGULAR_NPTH2, F.Cu at (71.1, 127.0)
- added U180: BREADBOARD_NPTH, mykicadlibs:TEST_BREADBOARD_RECTANGULAR_NPTH2, F.Cu at (58.4, 81.3)
- added U181: BREADBOARD_NPTH, mykicadlibs:TEST_BREADBOARD_RECTANGULAR_NPTH2, F.Cu at (61.0, 121.9)
- added U182: BREADBOARD_NPTH, mykicadlibs:TEST_BREADBOARD_RECTANGULAR_NPTH2, F.Cu at (71.1, 129.5)
- added U183: BREADBOARD_NPTH, mykicadlibs:TEST_BREADBOARD_RECTANGULAR_NPTH2, F.Cu at (63.5, 114.3)
- added U184: BREADBOARD_NPTH, mykicadlibs:TEST_BREADBOARD_RECTANGULAR_NPTH2, F.Cu at (66.0, 109.2)
- added U185: BREADBOARD_NPTH, mykicadlibs:TEST_BREADBOARD_RECTANGULAR_NPTH2, F.Cu at (68.6, 106.7)
- added U186: BREADBOARD_NPTH, mykicadlibs:TEST_BREADBOARD_RECTANGULAR_NPTH2, F.Cu at (71.1, 132.1)
- added U187: BREADBOARD_NPTH, mykicadlibs:TEST_BREADBOARD_RECTANGULAR_NPTH2, F.Cu at (71.1, 86.4)
- added U188: BREADBOARD_NPTH, mykicadlibs:TEST_BREADBOARD_RECTANGULAR_NPTH2, F.Cu at (50.8, 121.9)
- added U189: BREADBOARD_NPTH, mykicadlibs:TEST_BREADBOARD_RECTANGULAR_NPTH2, F.Cu at (53.3, 127.0)
- added U19: BREADBOARD_NPTH, mykicadlibs:TEST_BREADBOARD_RECTANGULAR_NPTH2, F.Cu at (48.3, 121.9)
- added U190: BREADBOARD_NPTH, mykicadlibs:TEST_BREADBOARD_RECTANGULAR_NPTH2, F.Cu at (50.8, 137.2)
- added U191: BREADBOARD_NPTH, mykicadlibs:TEST_BREADBOARD_RECTANGULAR_NPTH2, F.Cu at (58.4, 96.5)
- added U192: BREADBOARD_NPTH, mykicadlibs:TEST_BREADBOARD_RECTANGULAR_NPTH2, F.Cu at (58.4, 132.1)
- added U193: BREADBOARD_NPTH, mykicadlibs:TEST_BREADBOARD_RECTANGULAR_NPTH2, F.Cu at (58.4, 86.4)
- added U194: BREADBOARD_NPTH, mykicadlibs:TEST_BREADBOARD_RECTANGULAR_NPTH2, F.Cu at (61.0, 96.5)
- added U195: BREADBOARD_NPTH, mykicadlibs:TEST_BREADBOARD_RECTANGULAR_NPTH2, F.Cu at (63.5, 124.5)
- added U196: BREADBOARD_NPTH, mykicadlibs:TEST_BREADBOARD_RECTANGULAR_NPTH2, F.Cu at (66.0, 91.4)
- added U197: BREADBOARD_NPTH, mykicadlibs:TEST_BREADBOARD_RECTANGULAR_NPTH2, F.Cu at (66.0, 86.4)
- added U198: BREADBOARD_NPTH, mykicadlibs:TEST_BREADBOARD_RECTANGULAR_NPTH2, F.Cu at (68.6, 94.0)
- added U199: BREADBOARD_NPTH, mykicadlibs:TEST_BREADBOARD_RECTANGULAR_NPTH2, F.Cu at (48.3, 139.7)
- added U2: BREADBOARD_NPTH, mykicadlibs:TEST_BREADBOARD_RECTANGULAR_NPTH2, F.Cu at (48.3, 91.4)
- added U20: BREADBOARD_NPTH, mykicadlibs:TEST_BREADBOARD_RECTANGULAR_NPTH2, F.Cu at (48.3, 101.6)
- added U200: BREADBOARD_NPTH, mykicadlibs:TEST_BREADBOARD_RECTANGULAR_NPTH2, F.Cu at (53.3, 139.7)
- added U201: BREADBOARD_NPTH, mykicadlibs:TEST_BREADBOARD_RECTANGULAR_NPTH2, F.Cu at (55.9, 119.4)
- added U202: BREADBOARD_NPTH, mykicadlibs:TEST_BREADBOARD_RECTANGULAR_NPTH2, F.Cu at (53.3, 91.4)
- added U203: BREADBOARD_NPTH, mykicadlibs:TEST_BREADBOARD_RECTANGULAR_NPTH2, F.Cu at (55.9, 114.3)
- added U204: BREADBOARD_NPTH, mykicadlibs:TEST_BREADBOARD_RECTANGULAR_NPTH2, F.Cu at (58.4, 119.4)
- added U205: BREADBOARD_NPTH, mykicadlibs:TEST_BREADBOARD_RECTANGULAR_NPTH2, F.Cu at (58.4, 101.6)
- added U206: BREADBOARD_NPTH, mykicadlibs:TEST_BREADBOARD_RECTANGULAR_NPTH2, F.Cu at (61.0, 91.4)
- added U207: BREADBOARD_NPTH, mykicadlibs:TEST_BREADBOARD_RECTANGULAR_NPTH2, F.Cu at (63.5, 88.9)
- added U208: BREADBOARD_NPTH, mykicadlibs:TEST_BREADBOARD_RECTANGULAR_NPTH2, F.Cu at (66.0, 139.7)
- added U209: BREADBOARD_NPTH, mykicadlibs:TEST_BREADBOARD_RECTANGULAR_NPTH2, F.Cu at (68.6, 99.1)
- added U21: BREADBOARD_NPTH, mykicadlibs:TEST_BREADBOARD_RECTANGULAR_NPTH2, F.Cu at (66.0, 88.9)
- added U210: BREADBOARD_NPTH, mykicadlibs:TEST_BREADBOARD_RECTANGULAR_NPTH2, F.Cu at (55.9, 109.2)
- added U211: BREADBOARD_NPTH, mykicadlibs:TEST_BREADBOARD_RECTANGULAR_NPTH2, F.Cu at (50.8, 116.8)
- added U212: BREADBOARD_NPTH, mykicadlibs:TEST_BREADBOARD_RECTANGULAR_NPTH2, F.Cu at (53.3, 124.5)
- added U213: BREADBOARD_NPTH, mykicadlibs:TEST_BREADBOARD_RECTANGULAR_NPTH2, F.Cu at (53.3, 114.3)
- added U214: BREADBOARD_NPTH, mykicadlibs:TEST_BREADBOARD_RECTANGULAR_NPTH2, F.Cu at (55.9, 124.5)
- added U215: BREADBOARD_NPTH, mykicadlibs:TEST_BREADBOARD_RECTANGULAR_NPTH2, F.Cu at (58.4, 137.2)
- added U216: BREADBOARD_NPTH, mykicadlibs:TEST_BREADBOARD_RECTANGULAR_NPTH2, F.Cu at (61.0, 134.6)
- added U217: BREADBOARD_NPTH, mykicadlibs:TEST_BREADBOARD_RECTANGULAR_NPTH2, F.Cu at (63.5, 137.2)
- added U218: BREADBOARD_NPTH, mykicadlibs:TEST_BREADBOARD_RECTANGULAR_NPTH2, F.Cu at (63.5, 127.0)
- added U219: BREADBOARD_NPTH, mykicadlibs:TEST_BREADBOARD_RECTANGULAR_NPTH2, F.Cu at (66.0, 119.4)
- added U22: BREADBOARD_NPTH, mykicadlibs:TEST_BREADBOARD_RECTANGULAR_NPTH2, F.Cu at (63.5, 111.8)
- added U220: BREADBOARD_NPTH, mykicadlibs:TEST_BREADBOARD_RECTANGULAR_NPTH2, F.Cu at (68.6, 134.6)
- added U221: BREADBOARD_NPTH, mykicadlibs:TEST_BREADBOARD_RECTANGULAR_NPTH2, F.Cu at (68.6, 83.8)
- added U222: BREADBOARD_NPTH, mykicadlibs:TEST_BREADBOARD_RECTANGULAR_NPTH2, F.Cu at (53.3, 106.7)
- added U223: BREADBOARD_NPTH, mykicadlibs:TEST_BREADBOARD_RECTANGULAR_NPTH2, F.Cu at (50.8, 83.8)
- added U224: BREADBOARD_NPTH, mykicadlibs:TEST_BREADBOARD_RECTANGULAR_NPTH2, F.Cu at (55.9, 106.7)
- added U225: BREADBOARD_NPTH, mykicadlibs:TEST_BREADBOARD_RECTANGULAR_NPTH2, F.Cu at (58.4, 121.9)
- added U226: BREADBOARD_NPTH, mykicadlibs:TEST_BREADBOARD_RECTANGULAR_NPTH2, F.Cu at (58.4, 104.1)
- added U227: BREADBOARD_NPTH, mykicadlibs:TEST_BREADBOARD_RECTANGULAR_NPTH2, F.Cu at (55.9, 104.1)
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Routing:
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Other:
- board text added: "DRC violations will appear as the footprints for the breadboard have non-plated holes but connected pads. KiCad has currently no way to do this without DRC violations. Unconnected count must be 0."
